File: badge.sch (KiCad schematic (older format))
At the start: 123 parts, among them P1 CONN_8, P2 CONN_11

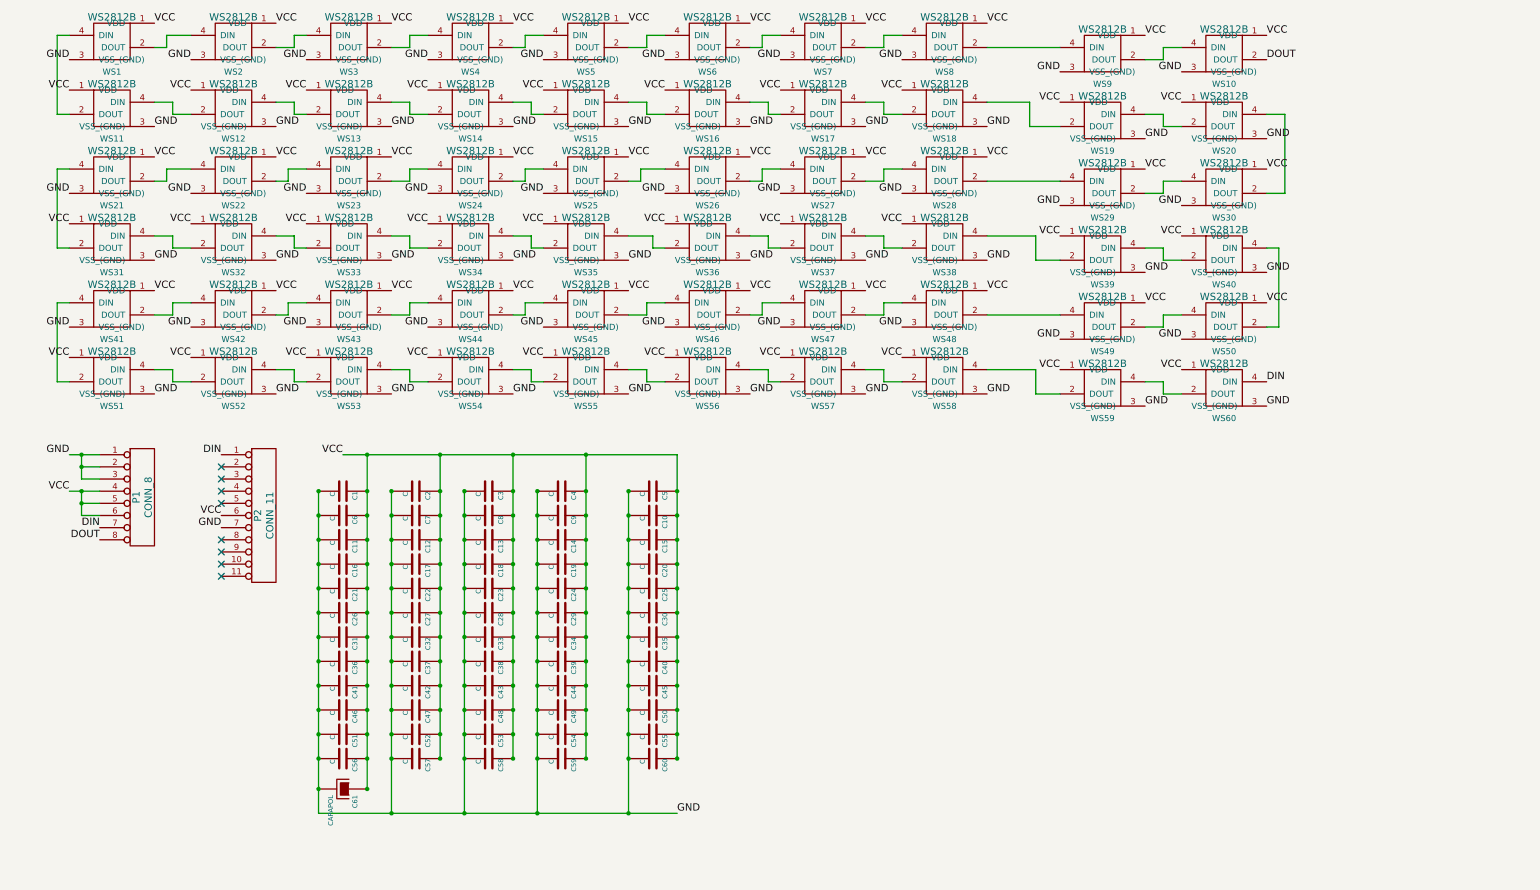
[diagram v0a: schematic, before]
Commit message: sch was broken, corrected
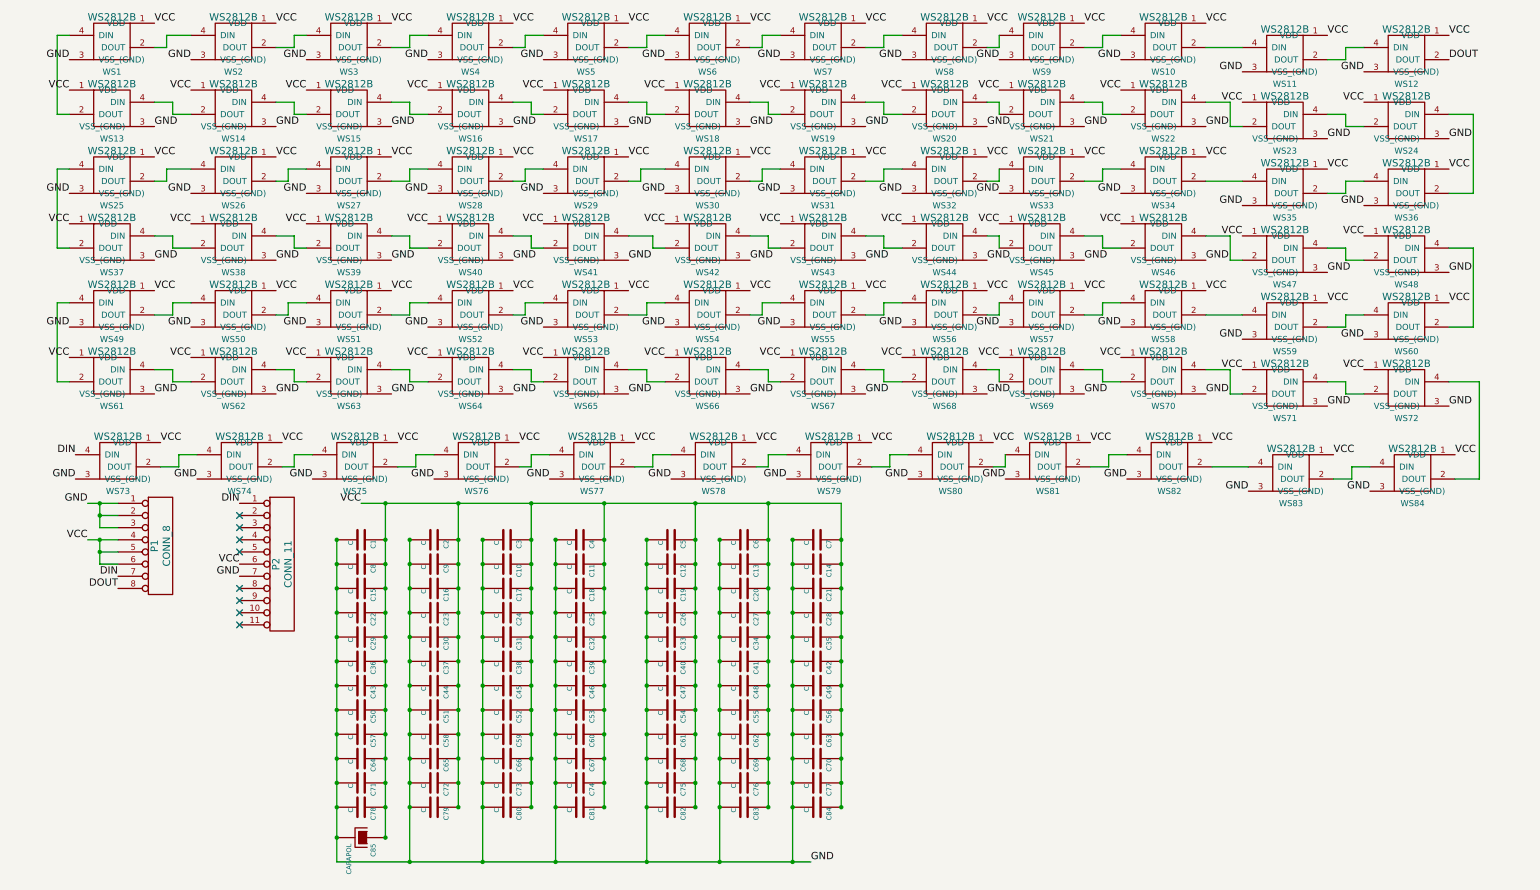
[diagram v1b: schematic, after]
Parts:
- added C13, C14, C20, C21, C27, C28, C34, C35, C41, C42, C48, C49, C55, C56, C6, C62, C63, C69, C7, C70, C76, C77, C83, C84: C, Capacitors_SMD:C_0805_HandSoldering, symbol C
- added WS11, WS12, WS23, WS24, WS35, WS36, WS47, WS48, WS59, WS60, WS71, WS72, WS73, WS74, WS75, WS76, WS77, WS78, WS79, WS80, WS81, WS82, WS83, WS84: WS2812B, badge:WS2812B, symbol WS2812B
- renumbered C8 to C10, C9 to C11, C10 to C12, C11 to C15, C12 to C16, C13 to C17, C14 to C18, C15 to C19, C16 to C22, C17 to C23, C18 to C24, C19 to C25, C20 to C26, C21 to C29, C22 to C30, C23 to C31, C24 to C32, C25 to C33, C26 to C36, C27 to C37, C28 to C38, C29 to C39, C30 to C40, C31 to C43, C32 to C44, C33 to C45, C34 to C46, C35 to C47, C36 to C50, C37 to C51, C38 to C52, C39 to C53, C40 to C54, C41 to C57, C42 to C58, C43 to C59, C44 to C60, C45 to C61, C46 to C64, C47 to C65, C48 to C66, C49 to C67, C50 to C68, C51 to C71, C52 to C72, C53 to C73, C54 to C74, C55 to C75, C56 to C78, C57 to C79, C6 to C8, C58 to C80, C59 to C81, C60 to C82, C61 to C85, C7 to C9, WS11 to WS13, WS12 to WS14, WS13 to WS15, WS14 to WS16, WS15 to WS17, WS16 to WS18, WS17 to WS19, WS18 to WS20, WS19 to WS21, WS20 to WS22, WS21 to WS25, WS22 to WS26, WS23 to WS27, WS24 to WS28, WS25 to WS29, WS26 to WS30, WS27 to WS31, WS28 to WS32, WS29 to WS33, WS30 to WS34, WS31 to WS37, WS32 to WS38, WS33 to WS39, WS34 to WS40, WS35 to WS41, WS36 to WS42, WS37 to WS43, WS38 to WS44, WS39 to WS45, WS40 to WS46, WS41 to WS49, WS42 to WS50, WS43 to WS51, WS44 to WS52, WS45 to WS53, WS46 to WS54, WS47 to WS55, WS48 to WS56, WS49 to WS57, WS50 to WS58, WS51 to WS61, WS52 to WS62, WS53 to WS63, WS54 to WS64, WS55 to WS65, WS56 to WS66, WS57 to WS67, WS58 to WS68, WS59 to WS69, WS60 to WS70
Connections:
- net DIN: now also WS73.4 (DIN); no longer WS70.4 (DIN)
- net DOUT: now also WS12.2 (DOUT); no longer WS10.2 (DOUT)
- net GND: now also C13.2, C14.2, C20.2, C21.2, C27.2, C28.2, C34.2, C35.2, C41.2, C42.2, C48.2, C49.2, C55.2, C56.2, C6.2, C62.2, C63.2, C69.2, C7.2, C70.2, C76.2, C77.2, C83.2, C84.2, WS11.3 (VSS_(GND)), WS12.3 (VSS_(GND)), WS23.3 (VSS_(GND)), WS24.3 (VSS_(GND)), WS35.3 (VSS_(GND)), WS36.3 (VSS_(GND)), WS47.3 (VSS_(GND)), WS48.3 (VSS_(GND)), WS59.3 (VSS_(GND)), WS60.3 (VSS_(GND)), WS71.3 (VSS_(GND)), WS72.3 (VSS_(GND)), WS73.3 (VSS_(GND)), WS74.3 (VSS_(GND)), WS75.3 (VSS_(GND)), WS76.3 (VSS_(GND)), WS77.3 (VSS_(GND)), WS78.3 (VSS_(GND)), WS79.3 (VSS_(GND)), WS80.3 (VSS_(GND)), WS81.3 (VSS_(GND)), WS82.3 (VSS_(GND)), WS83.3 (VSS_(GND)), WS84.3 (VSS_(GND))
- net VCC: now also C13.1, C14.1, C20.1, C21.1, C27.1, C28.1, C34.1, C35.1, C41.1, C42.1, C48.1, C49.1, C55.1, C56.1, C6.1, C62.1, C63.1, C69.1, C7.1, C70.1, C76.1, C77.1, C83.1, C84.1, WS11.1 (VDD), WS12.1 (VDD), WS23.1 (VDD), WS24.1 (VDD), WS35.1 (VDD), WS36.1 (VDD), WS47.1 (VDD), WS48.1 (VDD), WS59.1 (VDD), WS60.1 (VDD), WS71.1 (VDD), WS72.1 (VDD), WS73.1 (VDD), WS74.1 (VDD), WS75.1 (VDD), WS76.1 (VDD), WS77.1 (VDD), WS78.1 (VDD), WS79.1 (VDD), WS80.1 (VDD), WS81.1 (VDD), WS82.1 (VDD), WS83.1 (VDD), WS84.1 (VDD)
- net at WS22.4 (DIN): now also WS23.2 (DOUT); no longer WS34.2 (DOUT)
- net at WS46.4 (DIN): now also WS47.2 (DOUT); no longer WS58.2 (DOUT)
- new net: WS10.2 (DOUT), WS11.4 (DIN)
- new net: WS34.2 (DOUT), WS35.4 (DIN)
- new net: WS58.2 (DOUT), WS59.4 (DIN)
- new net: WS70.4 (DIN), WS71.2 (DOUT)
- new net: WS73.2 (DOUT), WS74.4 (DIN)
- new net: WS74.2 (DOUT), WS75.4 (DIN)
- new net: WS75.2 (DOUT), WS76.4 (DIN)
- new net: WS76.2 (DOUT), WS77.4 (DIN)
- new net: WS77.2 (DOUT), WS78.4 (DIN)
- new net: WS78.2 (DOUT), WS79.4 (DIN)
- new net: WS79.2 (DOUT), WS80.4 (DIN)
- new net: WS80.2 (DOUT), WS81.4 (DIN)
- new net: WS81.2 (DOUT), WS82.4 (DIN)
- new net: WS82.2 (DOUT), WS83.4 (DIN)
- new net: WS11.2 (DOUT), WS12.4 (DIN)
- new net: WS23.4 (DIN), WS24.2 (DOUT)
- new net: WS35.2 (DOUT), WS36.4 (DIN)
- new net: WS47.4 (DIN), WS48.2 (DOUT)
- new net: WS59.2 (DOUT), WS60.4 (DIN)
- new net: WS71.4 (DIN), WS72.2 (DOUT)
- new net: WS24.4 (DIN), WS36.2 (DOUT)
- new net: WS48.4 (DIN), WS60.2 (DOUT)
- new net: WS72.4 (DIN), WS84.2 (DOUT)
- new net: WS83.2 (DOUT), WS84.4 (DIN)
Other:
- moved on the sheet: C1, C10, C11, C12, C15, C16, C17, C18, C19, C2, C22, C23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

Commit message: Addition of second data input so we can unpopulate first and last row.
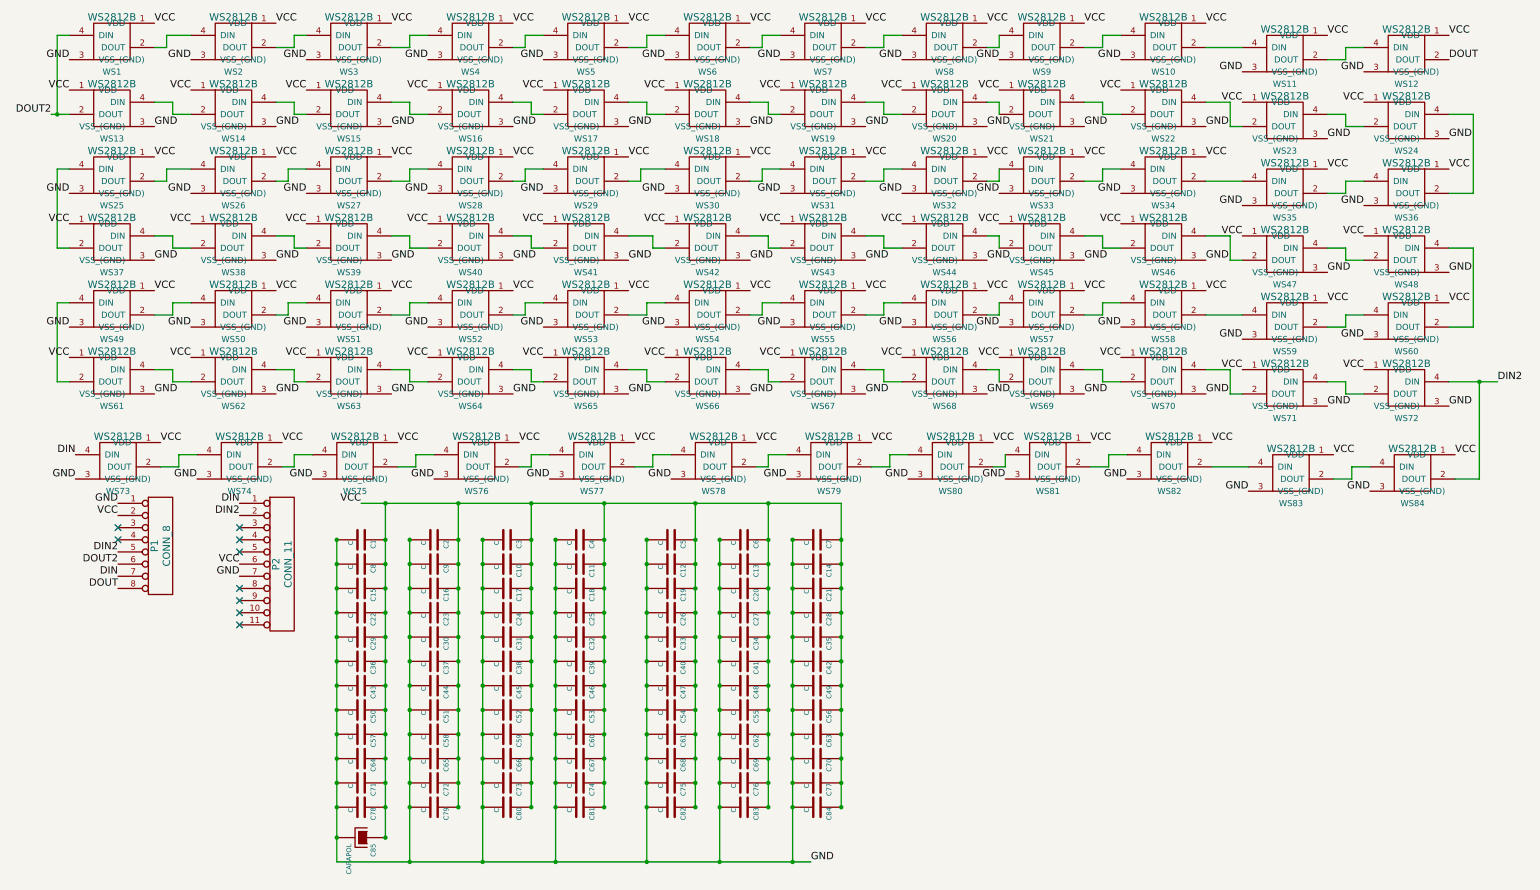
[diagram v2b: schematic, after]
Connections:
- net GND: no longer P1.2 (P2), P1.3 (P3)
- net VCC: now also P1.2 (P2); no longer P1.4 (P4), P1.5 (P5), P1.6 (P6)
- net DOUT2: now reaches WS1.4 (DIN), WS13.2 (DOUT)
- net DOUT2: now also P1.6 (P6)
- net DIN2: now reaches P2.2 (P2)
- net DIN2: now also P1.5 (P5), WS72.4 (DIN), WS84.2 (DOUT)
- no-connect marks 8 -> 9
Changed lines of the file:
@@
 	1550 1350 1400 1350
 Wire Wire Line
-	700  1450 600  1450
+	550  1450 700  1450
 Wire Wire Line
 	600  800  700  800
@@
 Connection ~ 4500 4650
 Connection ~ 3300 7150
-Wire Wire Line
-	950  4850 1100 4850
-Wire Wire Line
-	950  4650 950  4850
-Wire Wire Line
-	850  4650 1100 4650
-Connection ~ 950  4650
-Wire Wire Line
-	1100 4750 950  4750
-Connection ~ 950  4750
-Wire Wire Line
-	950  5150 1100 5150
-Wire Wire Line
-	950  4950 950  5150
-Wire Wire Line
-	850  4950 1100 4950
-Connection ~ 950  4950
-Wire Wire Line
-	1100 5050 950  5050
-Connection ~ 950  5050
-Text Label 850  4950 2    60   ~ 0
-VCC
-Text Label 850  4650 2    60   ~ 0
+Text Label 1100 4750 2    60   ~ 0
+VCC
+Text Label 1100 4650 2    60   ~ 0
 GND
 Text Label 1100 5250 2    60   ~ 0
@@
 Text Label 2100 4650 2    60   ~ 0
 DIN
-NoConn ~ 2100 4750
 NoConn ~ 2100 4850
 NoConn ~ 2100 4950
@@
 	12250 2550 12050 2550
 Wire Wire Line
-	12050 3650 12300 3650
+	12050 3650 12450 3650
 Wire Wire Line
 	12300 3650 12300 4450
@@
 Connection ~ 6050 7600
 Connection ~ 6650 7600
+Connection ~ 12300 3650
+Text Label 12450 3650 0    60   ~ 0
+DIN2
+Connection ~ 600  1450
+Text Label 550  1450 2    60   ~ 0
+DOUT2
+Text Label 1100 5150 2    60   ~ 0
+DOUT2
+Text Label 1100 5050 2    60   ~ 0
+DIN2
+Text Label 2100 4750 2    60   ~ 0
+DIN2
+NoConn ~ 1100 4850
+NoConn ~ 1100 4950
 $EndSCHEMATC
